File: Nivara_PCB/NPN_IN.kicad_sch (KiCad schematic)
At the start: 14 parts, among them Q1 IRLML6344, Q2 IRLML6344

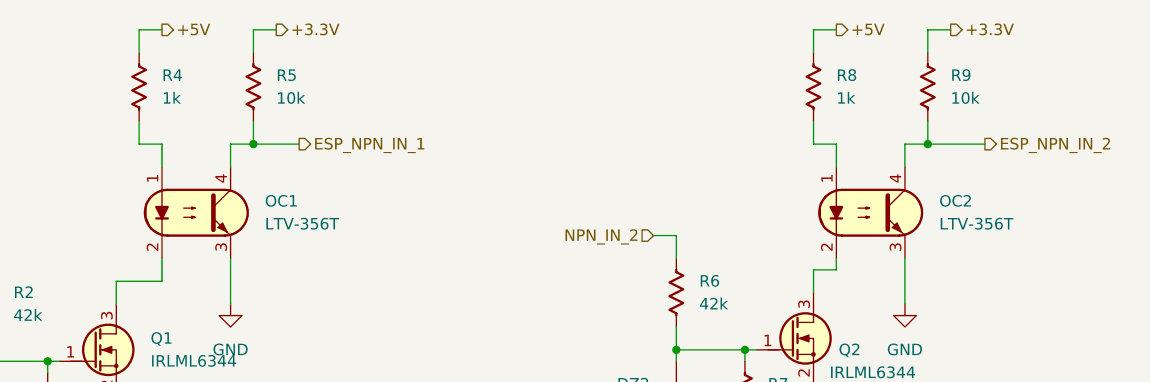
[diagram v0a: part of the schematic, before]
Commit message: Cambio de IntelliFet, porque los que tenían no estaban disponibles.
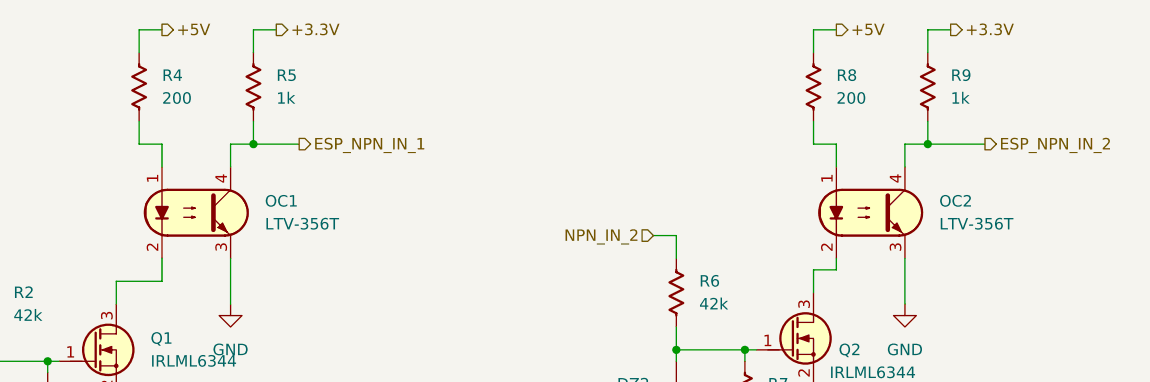
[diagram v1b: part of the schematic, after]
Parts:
- R4, R8: value 1k -> 200
- R5, R9: value 10k -> 1k
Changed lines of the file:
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@@
 			)
 		)
-		(property "Value" "1k"
+		(property "Value" "200"
 			(at 53.34 36.8299 0)
 			(effects
@@
 			)
 		)
-		(property "Value" "10k"
+		(property "Value" "1k"
 			(at 140.97 36.8299 0)
 			(effects
@@
 			)
 		)
-		(property "Value" "10k"
+		(property "Value" "1k"
 			(at 66.04 36.8299 0)
 			(effects
@@
 			)
 		)
-		(property "Value" "1k"
+		(property "Value" "200"
 			(at 128.27 36.8299 0)
 			(effects

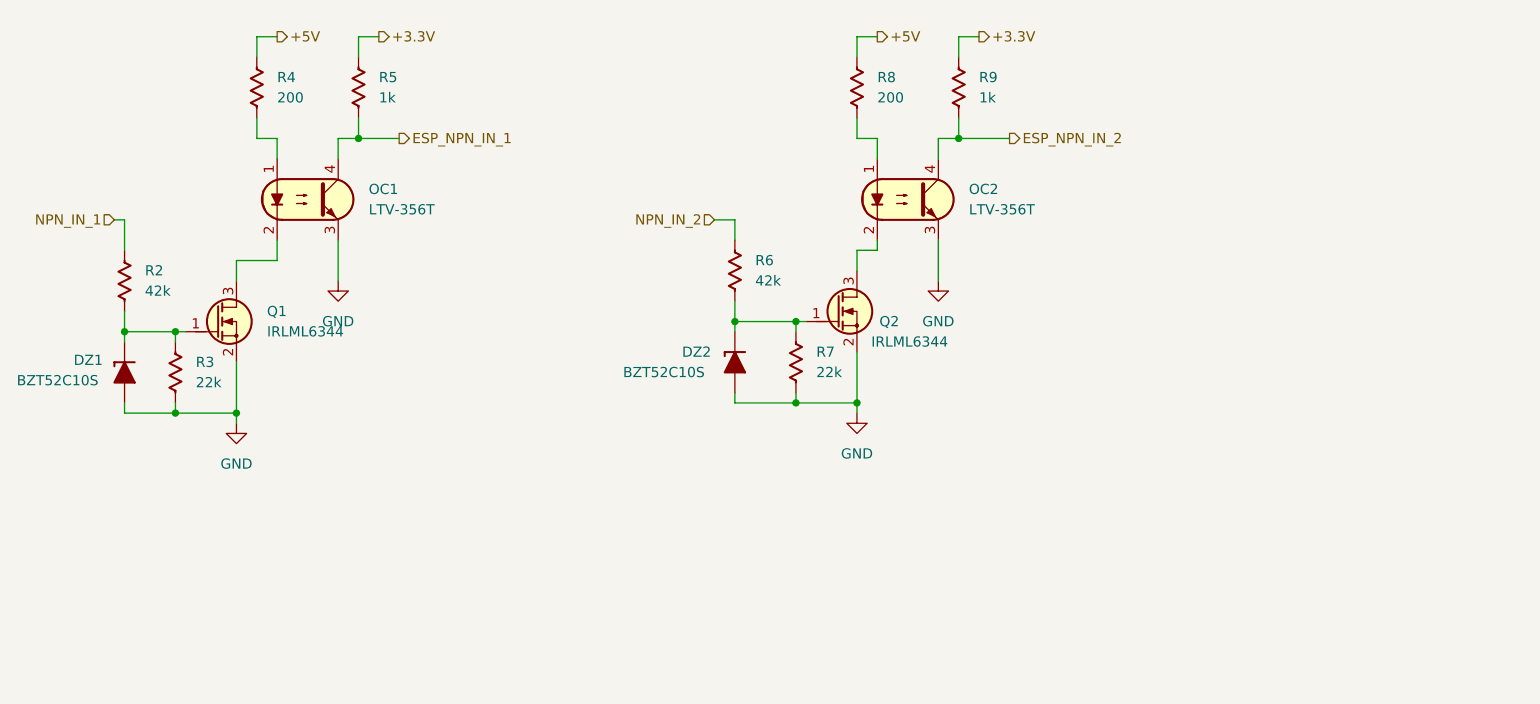
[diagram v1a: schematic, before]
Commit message: Cambios en las mediciones análogas.
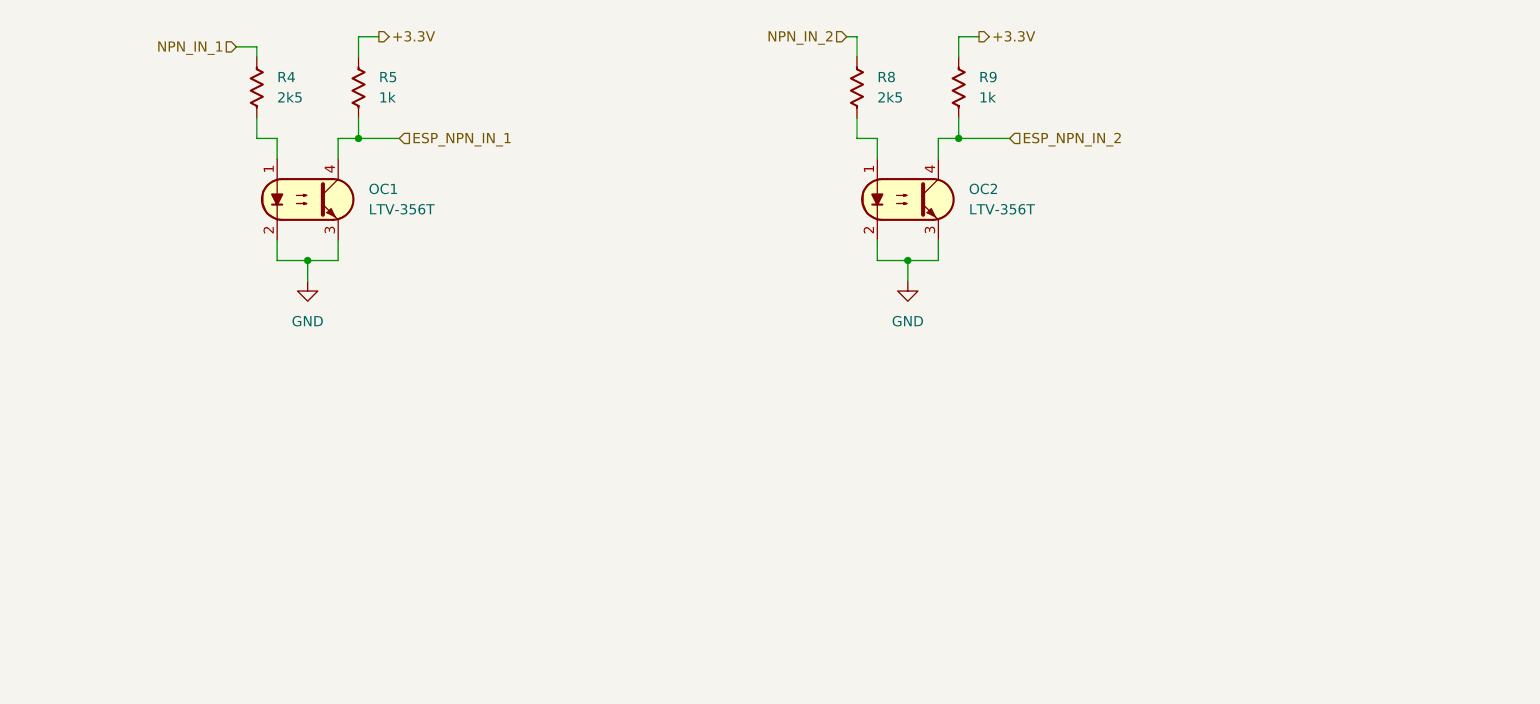
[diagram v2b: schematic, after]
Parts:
- removed DZ1, DZ2: BZT52C10S, PCM_Diode_SMD_AKL:D_SOD-323, symbol PCM_Diode_Zener_AKL:BZT52C10S
- removed Q1, Q2: IRLML6344, PCM_Package_TO_SOT_SMD_AKL:SOT-23, symbol PCM_Transistor_MOSFET_AKL:IRLML6344
- removed R2, R6: 42k, PCM_Resistor_SMD_AKL:R_0603_1608Metric, symbol PCM_Resistor_US_AKL:R_0603
- removed R3, R7: 22k, PCM_Resistor_SMD_AKL:R_0603_1608Metric, symbol PCM_Resistor_US_AKL:R_0603
- R4, R8: value 200 -> 2k5
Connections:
- net GND: now also OC1.2, OC2.2
- net NPN_IN_1: now also R4.1
- net NPN_IN_2: now also R8.1
- removed net +5V: R4.1, R8.1

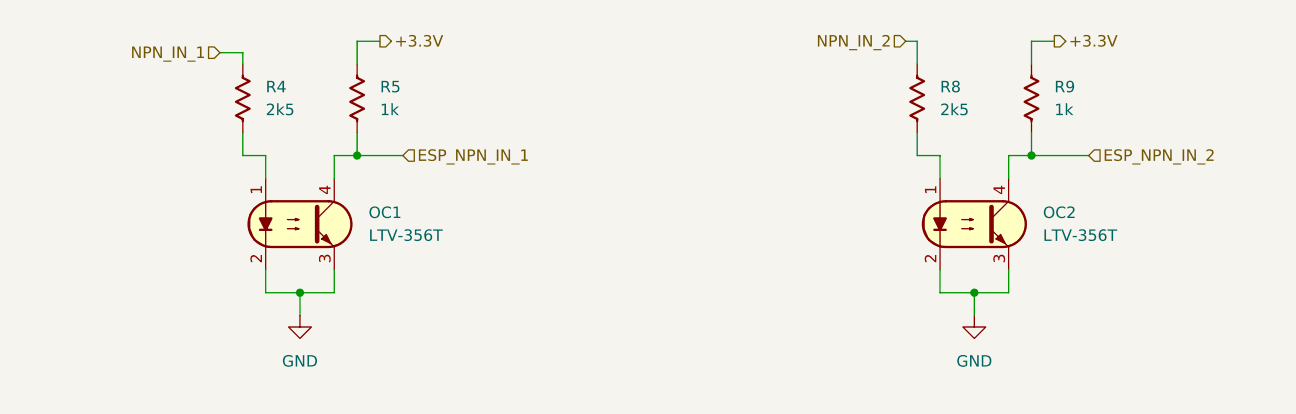
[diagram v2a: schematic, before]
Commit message: Cambios en las salidas analogicas, ya que el ESP32 S3 no tiene DAC
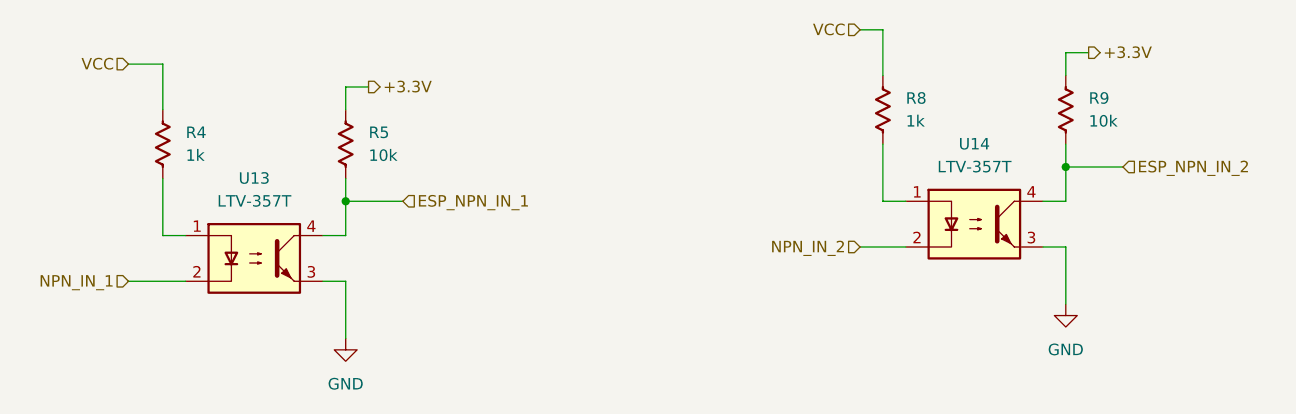
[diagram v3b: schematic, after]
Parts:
- removed OC1, OC2: LTV-356T, PCM_Package_SO_AKL:SO-4_4.4x3.9mm_P2.54mm, symbol PCM_Optocoupler_AKL:LTV-356T
- added U13, U14: LTV-357T, Package_SO:SO-4_4.4x3.6mm_P2.54mm, symbol Isolator:LTV-357T
- R4, R8: value 2k5 -> 1k
- R5, R9: value 1k -> 10k
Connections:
- net ESP_NPN_IN_1: now also U13.4
- net ESP_NPN_IN_2: now also U14.4
- net GND: now also U13.3, U14.3
- net NPN_IN_1: now also U13.2; no longer R4.1
- net NPN_IN_2: now also U14.2; no longer R8.1
- net at R4.2: now also U13.1
- net at R8.2: now also U14.1
- new net VCC: R4.1, R8.1
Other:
- moved on the sheet: R8, R9

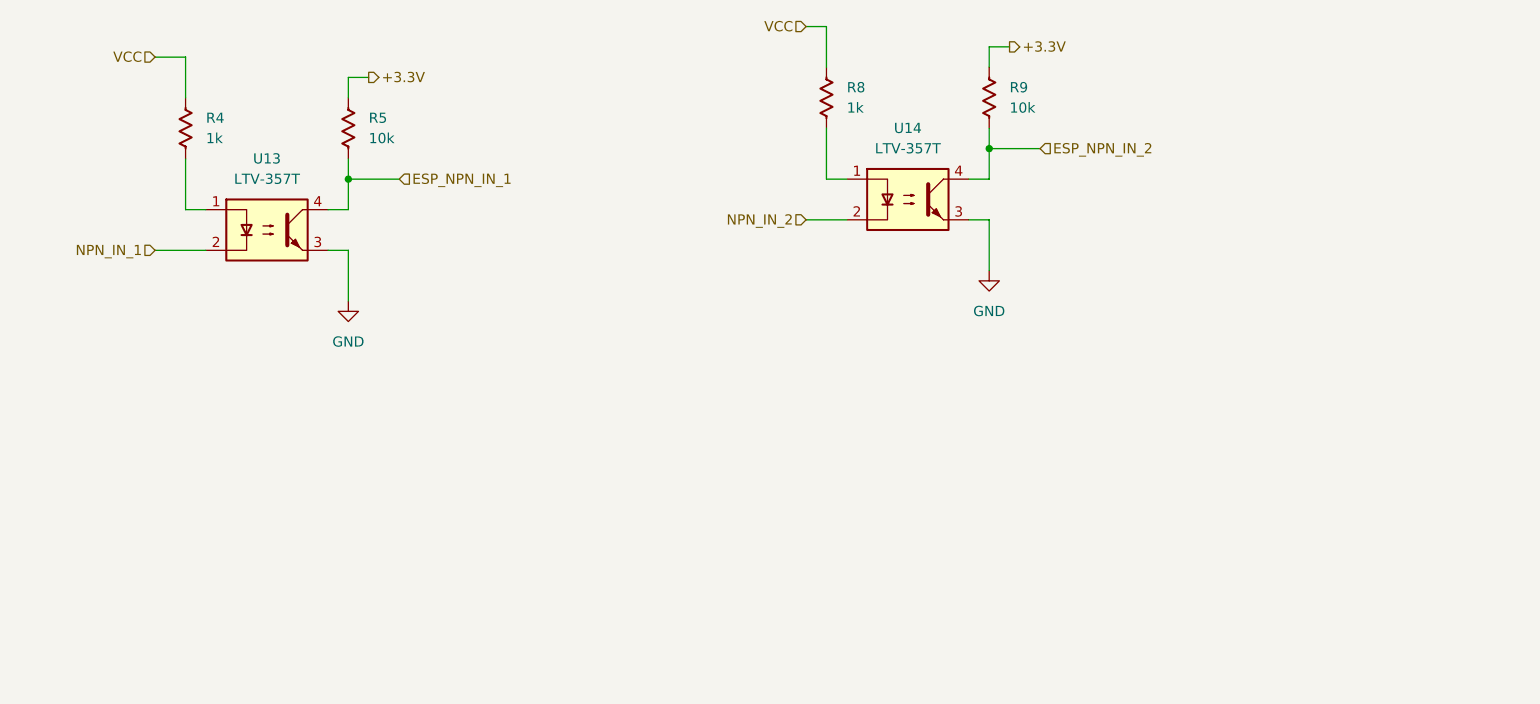
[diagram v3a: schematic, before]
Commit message: Cambios en la medición de voltaje y corriente de la PCB Nivara.
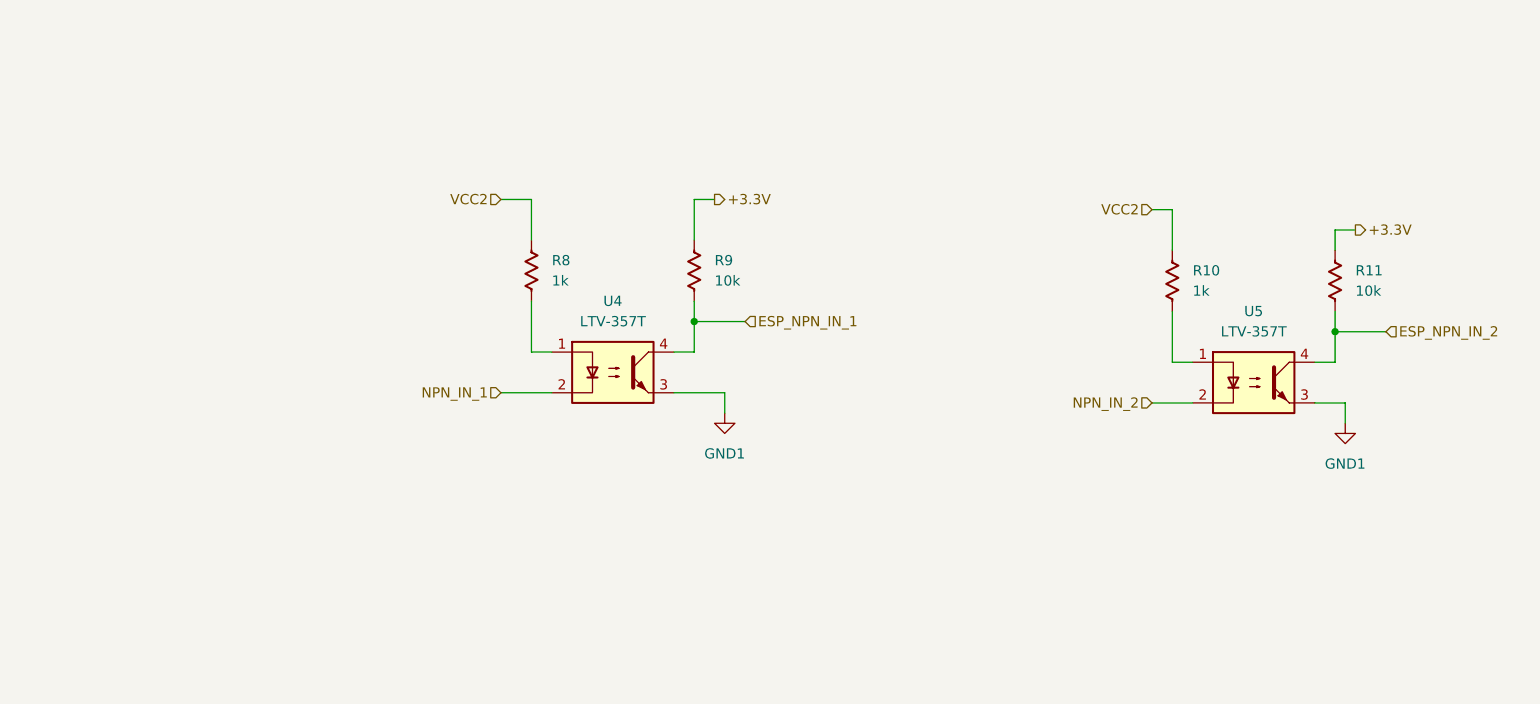
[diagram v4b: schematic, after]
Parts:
- renumbered R8 to R10, R9 to R11, R4 to R8, R5 to R9, U13 to U4, U14 to U5
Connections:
- net GND renamed GND1
- net VCC renamed VCC2
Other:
- moved on the sheet: R10, R11, R8, R9, U4, U5

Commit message: New changes to the Nivara PCB schematic files.
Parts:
- added D22, D26: LED ON, LED_SMD:LED_0603_1608Metric, symbol Device:LED
- R11, R9: value 10k -> 140
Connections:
- net ESP_NPN_IN_1: now also D26.1 (K); no longer R9.2
- net ESP_NPN_IN_2: now also D22.1 (K); no longer R11.2
- new net: D26.2 (A), R9.2
- new net: D22.2 (A), R11.2
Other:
- moved on the sheet: R10, R8

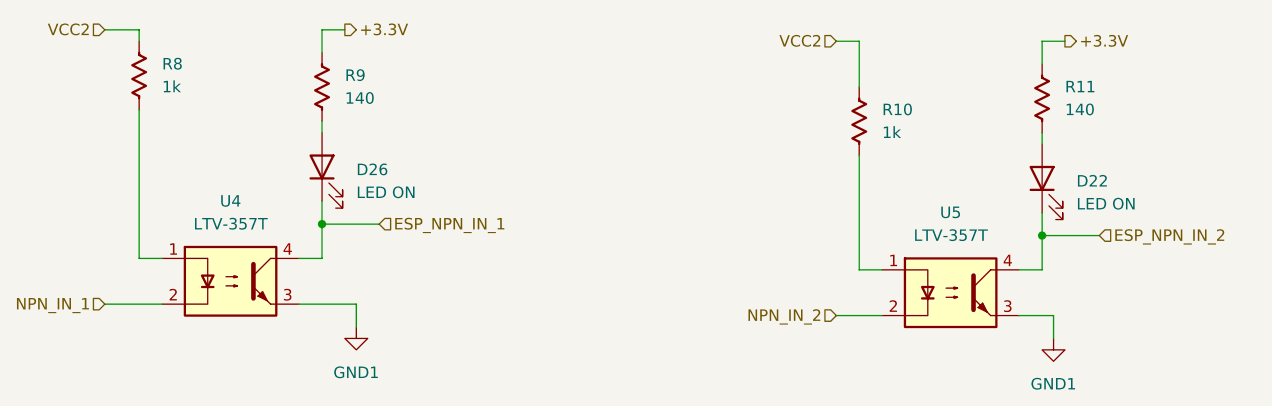
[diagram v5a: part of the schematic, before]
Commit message: Cambios en el PCB de Nivara. Ruteo de emtradas y salidas NPN y PNP.
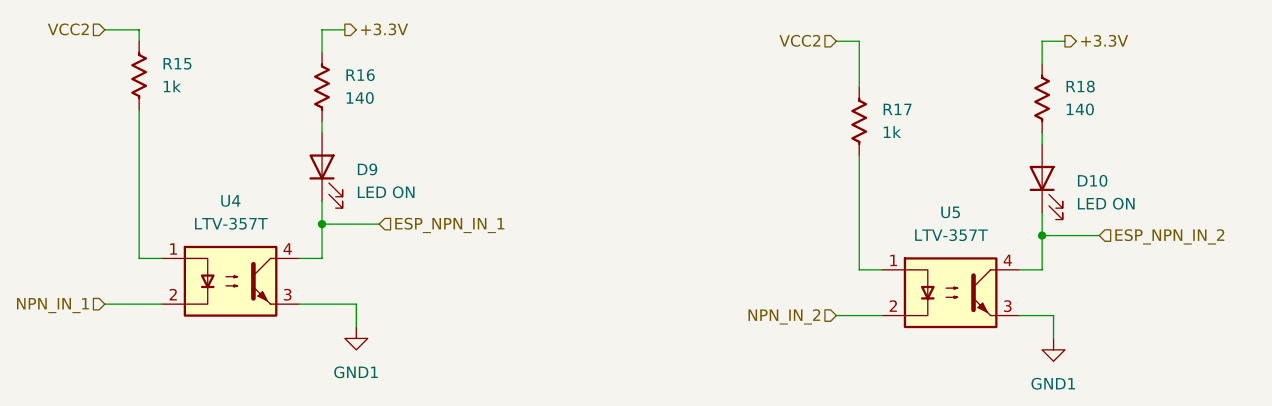
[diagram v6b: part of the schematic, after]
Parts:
- renumbered D22 to D10, D26 to D9, R8 to R15, R9 to R16, R10 to R17, R11 to R18
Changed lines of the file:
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@@
 		(dnp no)
 		(fields_autoplaced yes)
-		(property "Reference" "D26"
+		(property "Reference" "D9"
 			(at 109.22 58.7374 90)
 			(effects
@@
 			(project "Nivara_PCB"
 				(path "/13184db0-a71d-4054-b13a-bbf46d2b100d/4e7fa7f2-8bf5-4f9c-874d-fa1b4fd76f92/58467d6c-1433-4318-a1ea-3b041dc0b319"
-					(reference "D26")
+					(reference "D9")
 					(unit 1)
 				)
@@
 		(dnp no)
 		(fields_autoplaced yes)
-		(property "Reference" "R11"
+		(property "Reference" "R18"
 			(at 187.96 49.5299 0)
 			(effects
@@
 			(project "Nivara_PCB"
 				(path "/13184db0-a71d-4054-b13a-bbf46d2b100d/4e7fa7f2-8bf5-4f9c-874d-fa1b4fd76f92/58467d6c-1433-4318-a1ea-3b041dc0b319"
-					(reference "R11")
+					(reference "R18")
 					(unit 1)
 				)
@@
 		(dnp no)
 		(fields_autoplaced yes)
-		(property "Reference" "R8"
+		(property "Reference" "R15"
 			(at 87.63 46.9899 0)
 			(effects
@@
 			(project "Nivara_PCB"
 				(path "/13184db0-a71d-4054-b13a-bbf46d2b100d/4e7fa7f2-8bf5-4f9c-874d-fa1b4fd76f92/58467d6c-1433-4318-a1ea-3b041dc0b319"
-					(reference "R8")
+					(reference "R15")
 					(unit 1)
 				)
@@
 		(dnp no)
 		(fields_autoplaced yes)
-		(property "Reference" "R9"
+		(property "Reference" "R16"
 			(at 107.95 48.2599 0)
 			(effects
@@
 			(project "Nivara_PCB"
 				(path "/13184db0-a71d-4054-b13a-bbf46d2b100d/4e7fa7f2-8bf5-4f9c-874d-fa1b4fd76f92/58467d6c-1433-4318-a1ea-3b041dc0b319"
-					(reference "R9")
+					(reference "R16")
 					(unit 1)
 				)
@@
 		(dnp no)
 		(fields_autoplaced yes)
-		(property "Reference" "#PWR027"
+		(property "Reference" "#PWR048"
 			(at 109.22 82.55 0)
 			(effects
@@
 			(project "Nivara_PCB"
 				(path "/13184db0-a71d-4054-b13a-bbf46d2b100d/4e7fa7f2-8bf5-4f9c-874d-fa1b4fd76f92/58467d6c-1433-4318-a1ea-3b041dc0b319"
-					(reference "#PWR027")
+					(reference "#PWR048")
 					(unit 1)
 				)
@@
 		(dnp no)
 		(fields_autoplaced yes)
-		(property "Reference" "#PWR028"
+		(property "Reference" "#PWR049"
 			(at 186.69 83.82 0)
 			(effects
@@
 			(project "Nivara_PCB"
 				(path "/13184db0-a71d-4054-b13a-bbf46d2b100d/4e7fa7f2-8bf5-4f9c-874d-fa1b4fd76f92/58467d6c-1433-4318-a1ea-3b041dc0b319"
-					(reference "#PWR028")
+					(reference "#PWR049")
 					(unit 1)
 				)
@@
 		(dnp no)
 		(fields_autoplaced yes)
-		(property "Reference" "R10"
+		(property "Reference" "R17"
 			(at 167.64 52.0699 0)
 			(effects
@@
 			(project "Nivara_PCB"
 				(path "/13184db0-a71d-4054-b13a-bbf46d2b100d/4e7fa7f2-8bf5-4f9c-874d-fa1b4fd76f92/58467d6c-1433-4318-a1ea-3b041dc0b319"
-					(reference "R10")
+					(reference "R17")
 					(unit 1)
 				)
@@
 		(dnp no)
 		(fields_autoplaced yes)
-		(property "Reference" "D22"
+		(property "Reference" "D10"
 			(at 189.23 60.0074 90)
 			(effects
@@
 			(project "Nivara_PCB"
 				(path "/13184db0-a71d-4054-b13a-bbf46d2b100d/4e7fa7f2-8bf5-4f9c-874d-fa1b4fd76f92/58467d6c-1433-4318-a1ea-3b041dc0b319"
-					(reference "D22")
-					(unit 1)
-				)
+					(reference "D10")
+					(unit 1)
+				)
